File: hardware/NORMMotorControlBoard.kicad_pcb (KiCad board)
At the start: 2 copper layers, 2 parts, among them SW1 Reset, U1 Arduino Nano 33 BLE

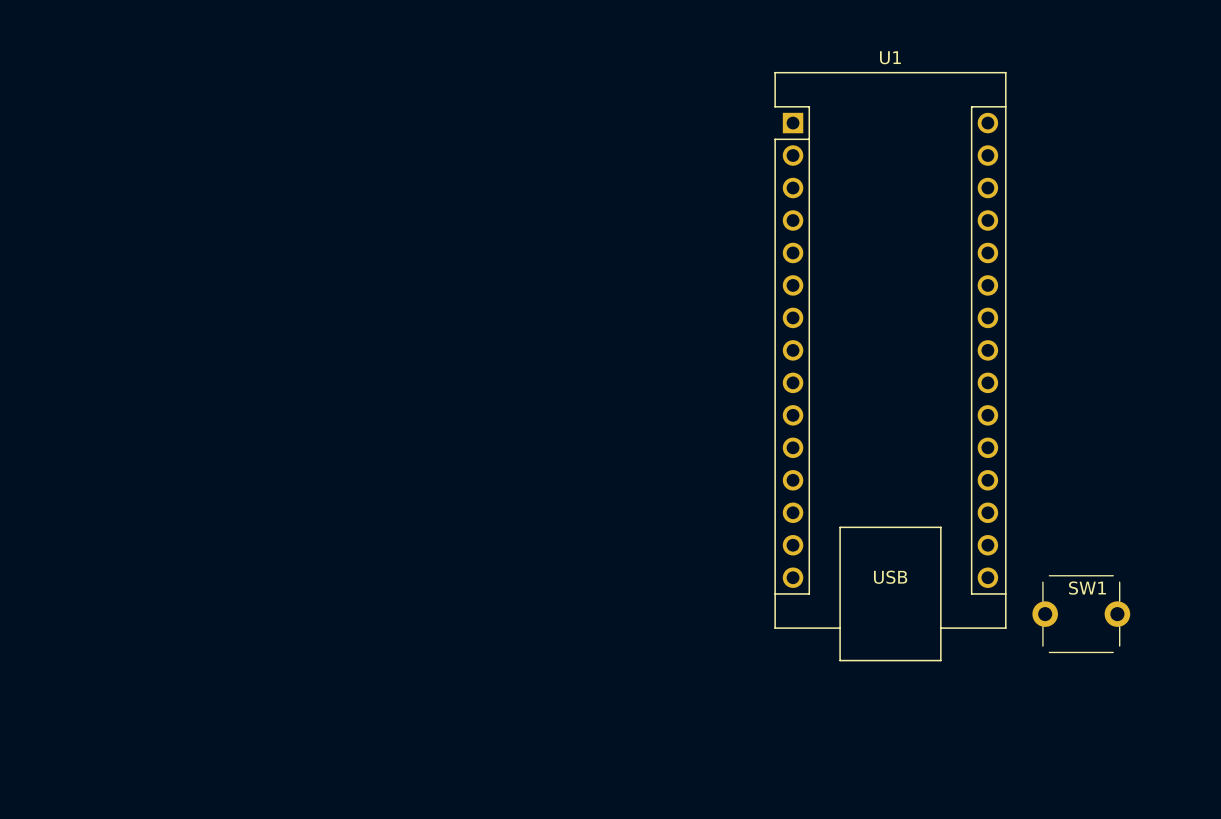
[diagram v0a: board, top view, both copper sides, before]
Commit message: Finished schematic and placed components
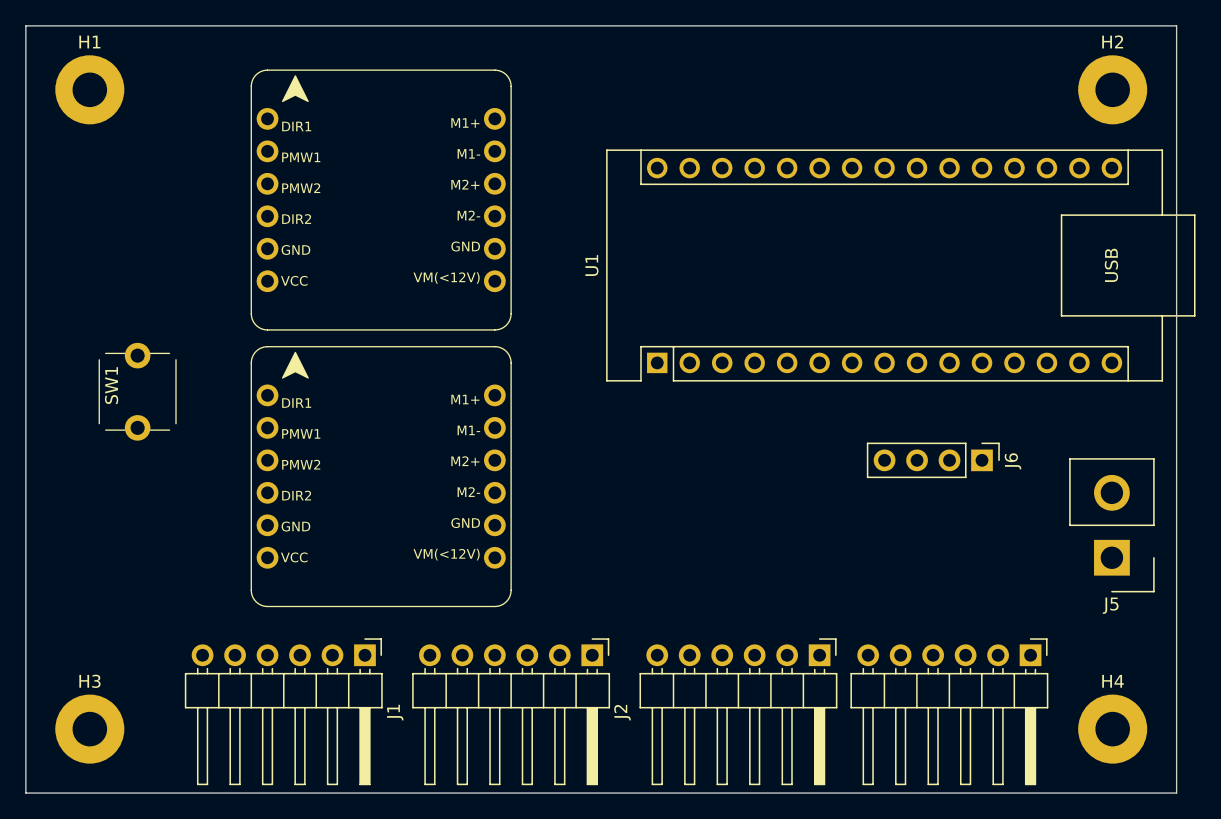
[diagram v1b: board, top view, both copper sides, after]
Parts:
- added H1: MountingHole_Pad, MountingHole:MountingHole_2.7mm_M2.5_Pad, F.Cu at (75.0, 65.0)
- added H2: MountingHole_Pad, MountingHole:MountingHole_2.7mm_M2.5_Pad, F.Cu at (155.0, 65.0)
- added H3: MountingHole_Pad, MountingHole:MountingHole_2.7mm_M2.5_Pad, F.Cu at (75.0, 115.0)
- added H4: MountingHole_Pad, MountingHole:MountingHole_2.7mm_M2.5_Pad, F.Cu at (155.0, 115.0)
- added J1: Front Left Motor, Connector_PinHeader_2.54mm:PinHeader_1x06_P2.54mm_Horizontal, F.Cu at (96.5, 109.2)
- added J2: Front Right Motor, Connector_PinHeader_2.54mm:PinHeader_1x06_P2.54mm_Horizontal, F.Cu at (114.3, 109.2)
- added J3: Back Left Motor, Connector_PinHeader_2.54mm:PinHeader_1x06_P2.54mm_Horizontal, F.Cu at (132.1, 109.2)
- added J4: Back Right Motor, Connector_PinHeader_2.54mm:PinHeader_1x06_P2.54mm_Horizontal, F.Cu at (148.6, 109.2)
- added J5: Conn_01x02_Socket, Connector_Samtec_HPM_THT:Samtec_HPM-02-01-x-S_Straight_1x02_Pitch5.08mm, F.Cu at (154.9, 101.6)
- added J6: Conn_01x04_Pin, Connector_PinHeader_2.54mm:PinHeader_1x04_P2.54mm_Vertical, F.Cu at (144.8, 94.0)
- added U2: Front Motors, DFRobot_DC_Motor_Driver_Shield:DFRobot_DC_Motor_Driver_Shield, F.Cu at (97.8, 95.3)
- added U3: Back Motors, DFRobot_DC_Motor_Driver_Shield:DFRobot_DC_Motor_Driver_Shield, F.Cu at (97.8, 73.7)
- moved SW1 75.8 mm to (78.7, 88.6), turned to 90 degrees
- moved U1 21.6 mm to (119.4, 86.4), turned to 90 degrees
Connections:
- U1 pad 15: unconnected-(U1-MISO-Pad15) -> D12
- U1 pad 16: unconnected-(U1-SCK-Pad16) -> D13
- U1 pad 23: unconnected-(U1-SDA/A4-Pad23) -> A4
- U1 pad 24: unconnected-(U1-SCL/A5-Pad24) -> A5
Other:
- board outline added: 90 x 60 mm

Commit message: Finished V1.0
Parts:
- moved J6 28.1 mm to (142.2, 66.0)
- moved U2 23.4 mm to (92.7, 72.4)
- moved U3 22.2 mm to (92.7, 95.3)
- moved SW1 2.54 mm to (76.2, 88.6), turned to 0 degrees
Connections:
- J6 pad 1: D12 -> D13
- J6 pad 2: D13 -> D12
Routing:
- net +5V: track 0.00 -> 254.7 mm
- net +3.3V: track 0.00 -> 105.9 mm
- net FL_ENC_B: track 0.00 -> 95.0 mm
- net FL_ENC_A: track 0.00 -> 92.5 mm
- net BL_DIR: track 0.00 -> 89.2 mm
- net BR_DIR: track 0.00 -> 75.5 mm
- net FR_ENC_B: track 0.00 -> 73.1 mm, vias 0 -> 1
- net FR_SPEED: track 0.00 -> 72.5 mm
- net FR_ENC_A: track 0.00 -> 70.5 mm, vias 0 -> 1
- net FR_DIR: track 0.00 -> 69.9 mm, vias 0 -> 1
- net FL_DIR: track 0.00 -> 68.0 mm
- net BR_SPEED: track 0.00 -> 59.5 mm
- net BL_SPEED: track 0.00 -> 56.6 mm
- net BL_ENC_B: track 0.00 -> 55.7 mm
- net FL_SPEED: track 0.00 -> 54.0 mm, vias 0 -> 1
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- added copper zone on B.Cu, net GND
- added copper zone on F.Cu, net GND
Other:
- outline, holes or cut-outs redrawn
- board text added: "(Neat Omnidirectional Robotic Module)"
- board text added: "5V"
- board text added: "A4"
- board text added: "A5"
- board text added: "Back Left"
- board text added: "Back Right"
- board text added: "D12"
- board text added: "D13"
- board text added: "ENC_A"
- board text added: "ENC_B"
- board text added: "Front Left"
- board text added: "Front Right"
- board text added: "GND"
- board text added: "M+"
- board text added: "M-"
- board text added: "N.O.R.M."
- board text added: "N.O.R.M. Motor Control Board github.com/HBoyd255/norm-motor-control-board V1.0 30/10/2024 Harry Boyd"
- board text added: "Project"
- board text added: "Reset"
- board text added: "VCC"

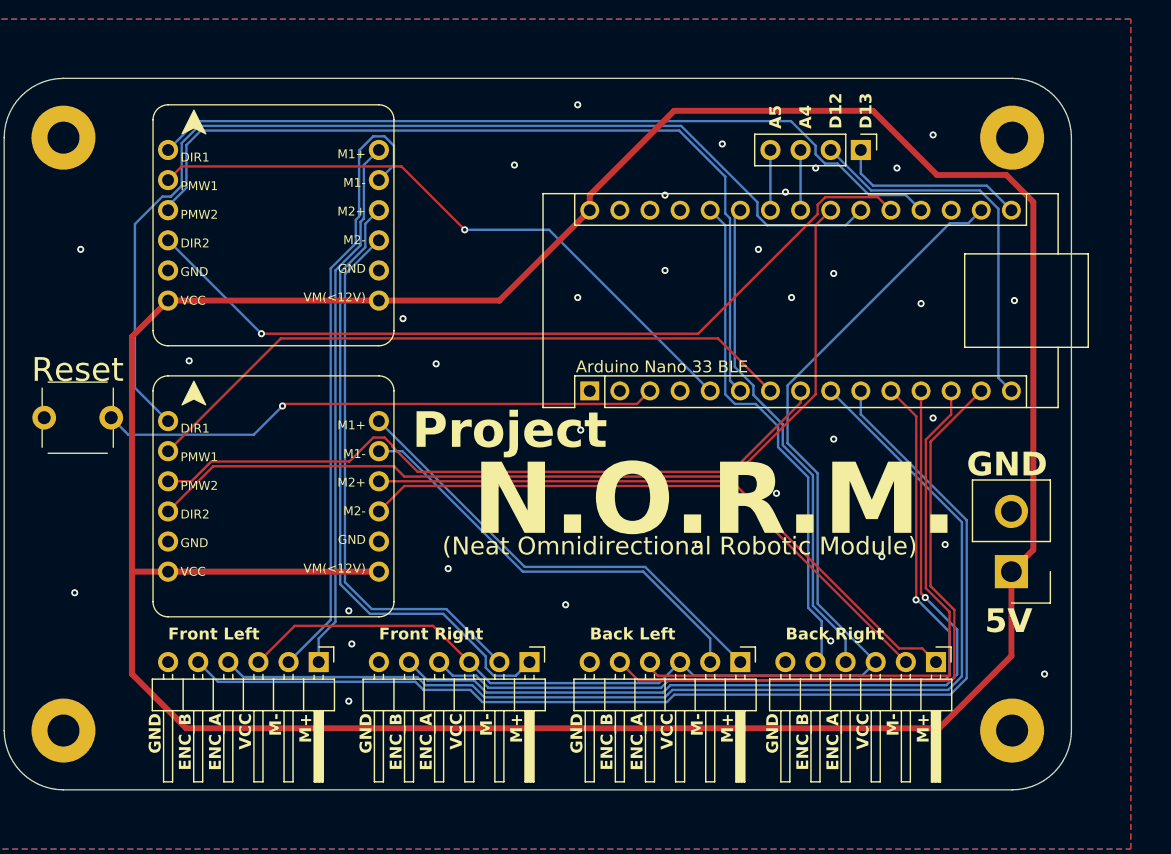
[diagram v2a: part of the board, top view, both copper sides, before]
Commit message: Added USB C and replaced components
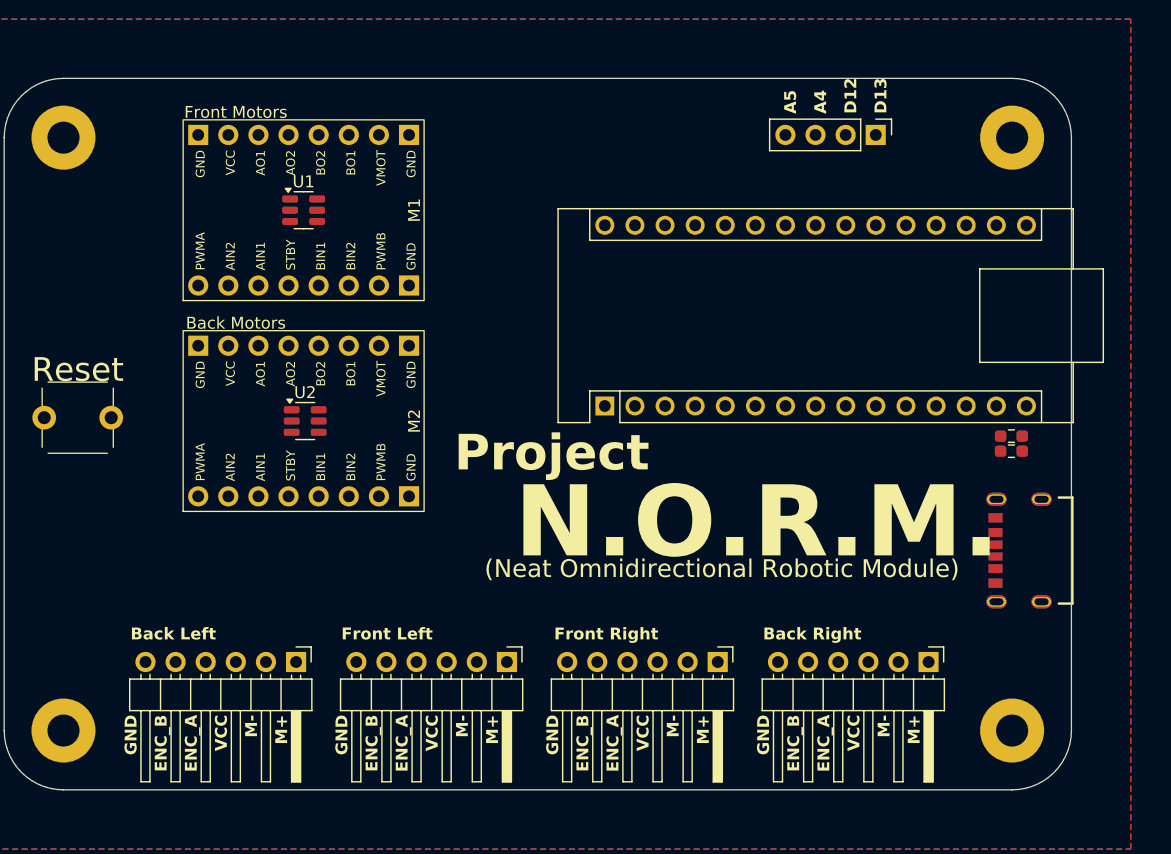
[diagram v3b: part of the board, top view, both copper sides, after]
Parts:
- removed the J2 at (114.3, 109.2)
- removed U3: Back Motors, DFRobot_DC_Motor_Driver_Shield:DFRobot_DC_Motor_Driver_Shield
- added A1: Arduino Nano 33 BLE, Module:Arduino_Nano, F.Cu at (120.7, 87.6)
- added J1: Back Left Motor, Connector_PinHeader_2.54mm:PinHeader_1x06_P2.54mm_Horizontal, F.Cu at (94.6, 109.2)
- added M1: Front Motors, Pololu_MD08A_Motor_Driver:Pololu_MD08A_Motor_Driver, F.Cu at (95.2, 71.1)
- added M2: Back Motors, Pololu_MD08A_Motor_Driver:Pololu_MD08A_Motor_Driver, F.Cu at (95.2, 88.9)
- added R3: 5.1k, Resistor_SMD:R_0603_1608Metric_Pad0.98x0.95mm_HandSolder, F.Cu at (154.9, 90.2)
- added R4: 5.1k, Resistor_SMD:R_0603_1608Metric_Pad0.98x0.95mm_HandSolder, F.Cu at (154.9, 91.4)
- J3: value Back Left Motor -> Front Right Motor
- J5: value Conn_01x02_Socket -> USB4125-GF-A_REVA2; footprint Connector_Samtec_HPM_THT:Samtec_HPM-02-01-x-S_Straight_1x02_Pitch5.08mm -> USB_C:USB_C
- U1: value Arduino Nano 33 BLE -> SN74LVC2G14DBV; footprint Module:Arduino_Nano -> Package_TO_SOT_SMD:SOT-23-6
- U2: value Front Motors -> SN74LVC2G14DBV; footprint DFRobot_DC_Motor_Driver_Shield:DFRobot_DC_Motor_Driver_Shield -> Package_TO_SOT_SMD:SOT-23-6
- moved U1 28.5 mm to (95.2, 71.1), turned to 0 degrees
- moved U2 16.7 mm to (95.4, 88.9)
- moved J2 15.9 mm to (112.4, 109.2)
- moved J5 2.49 mm to (156.7, 99.8), turned to 90 degrees
- moved J3 1.91 mm to (130.2, 109.2)
- moved J6 1.79 mm to (143.5, 64.8)
- moved J4 0.62 mm to (148.0, 109.2)
- renumbered J1 to J2
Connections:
- J2 pad 1: FL_M+ -> FR_M+
- J2 pad 2: FL_M- -> FR_M-
- J2 pad 4: FL_ENC_A -> FR_ENC_A
- J2 pad 5: FL_ENC_B -> FR_ENC_B
- SW1 pad 2: Net-(SW1-Pad2) -> Net-(A1-~{RESET}-Pad3)
- U1 pad 1: unconnected-(U1-TX1-Pad1) -> FL_DIR
- U1 pad 2: unconnected-(U1-RX1-Pad2) -> GND
- U1 pad 3: Net-(SW1-Pad2) -> FR_DIR
- U1 pad 4: GND -> /FR_DIR_INV
- U1 pad 5: FL_SPEED -> +5V
- U1 pad 6: FR_SPEED -> /FL_DIR_INV
- U2 pad 1: FL_DIR -> BL_DIR
- U2 pad 2: FL_SPEED -> GND
- U2 pad 3: FR_SPEED -> BR_DIR
- U2 pad 4: FR_DIR -> /BR_DIR_INV
- U2 pad 5: GND -> +5V
- U2 pad 6: +5V -> /BL_DIR_INV
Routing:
- net +5V: track 254.7 -> 0.00 mm
- net +3.3V: track 105.9 -> 0.00 mm
- net FL_ENC_B: track 95.0 -> 0.00 mm
- net FL_ENC_A: track 92.5 -> 0.00 mm
- net BL_DIR: track 89.2 -> 0.00 mm
- net BR_DIR: track 75.5 -> 0.00 mm
- net FR_ENC_B: track 73.1 -> 0.00 mm, vias 1 -> 0
- net FR_SPEED: track 72.5 -> 0.00 mm
- net FR_ENC_A: track 70.5 -> 0.00 mm, vias 1 -> 0
- net FR_DIR: track 69.9 -> 0.00 mm, vias 1 -> 0
- net FL_DIR: track 68.0 -> 0.00 mm
- net BR_SPEED: track 59.5 -> 0.00 mm
- net BL_SPEED: track 56.6 -> 0.00 mm
- net BL_ENC_B: track 55.7 -> 0.00 mm
- net FL_SPEED: track 54.0 -> 0.00 mm, vias 1 -> 0
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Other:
- board text added: "N.O.R.M. Motor Control Board github.com/HBoyd255/norm-motor-control-board V1.1 20/11/2024 Harry Boyd"
- board text removed: "5V"
- board text removed: "N.O.R.M. Motor Control Board github.com/HBoyd255/norm-motor-control-board V1.0 30/10/2024 Harry Boyd"

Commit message: Exported board v1.1
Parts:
- moved R4 0.38 mm to (154.9, 91.8)
- moved U1 0.13 mm to (95.4, 71.1)
- moved J5 0.09 mm to (156.6, 99.8)
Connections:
- J1 pad 1: FL_M+ -> BL_M+
- J1 pad 2: FL_M- -> BL_M-
- J1 pad 4: FL_ENC_A -> BL_ENC_A
- J1 pad 5: FL_ENC_B -> BL_ENC_B
- J2 pad 1: FR_M+ -> FL_M+
- J2 pad 2: FR_M- -> FL_M-
- J2 pad 4: FR_ENC_A -> FL_ENC_A
- J2 pad 5: FR_ENC_B -> FL_ENC_B
- J3 pad 1: BL_M+ -> FR_M+
- J3 pad 2: BL_M- -> FR_M-
- J3 pad 4: BL_ENC_A -> FR_ENC_A
- J3 pad 5: BL_ENC_B -> FR_ENC_B
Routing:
- net +3.3V: track 0.00 -> 202.1 mm
- net +5V: track 0.00 -> 131.2 mm, vias 0 -> 1
- net BL_DIR: track 0.00 -> 88.3 mm, vias 0 -> 2
- net Net-(A1-~{RESET}-Pad3): track 0.00 -> 88.0 mm
- net BL_ENC_B: track 0.00 -> 82.3 mm, vias 0 -> 1
- net FL_DIR: track 0.00 -> 77.1 mm, vias 0 -> 1
- net BL_ENC_A: track 0.00 -> 76.6 mm, vias 0 -> 1
- net BR_DIR: track 0.00 -> 71.1 mm, vias 0 -> 3
- net BL_SPEED: track 0.00 -> 64.7 mm, vias 0 -> 2
- net BR_M-: track 0.00 -> 62.4 mm
- net BR_M+: track 0.00 -> 61.5 mm
- net FL_M-: track 0.00 -> 60.6 mm
- net FR_DIR: track 0.00 -> 59.5 mm, vias 0 -> 2
- net FR_M-: track 0.00 -> 58.2 mm
- net FR_M+: track 0.00 -> 57.3 mm
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
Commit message: Placed components
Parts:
- removed M1: Front Motors, Pololu_MD08A_Motor_Driver:Pololu_MD08A_Motor_Driver
- removed M2: Back Motors, Pololu_MD08A_Motor_Driver:Pololu_MD08A_Motor_Driver
- added D1: LED, LED_SMD:LED_0603_1608Metric, F.Cu at (262.9, 188.7)
- added D2: LED, LED_SMD:LED_0603_1608Metric, F.Cu at (265.4, 188.7)
- added D3: LED, LED_SMD:LED_0603_1608Metric, F.Cu at (268.0, 188.7)
- added D4: LED, LED_SMD:LED_0603_1608Metric, F.Cu at (270.5, 188.7)
- added D5: LED, LED_SMD:LED_0603_1608Metric, F.Cu at (254.0, 230.8)
- added D6: LED, LED_SMD:LED_0603_1608Metric, F.Cu at (251.5, 230.8)
- added D7: LED, LED_SMD:LED_0603_1608Metric, F.Cu at (248.9, 230.8)
- added D8: LED, LED_SMD:LED_0603_1608Metric, F.Cu at (246.4, 230.8)
- added J7: SparePins, Connector_PinHeader_2.54mm:PinHeader_1x05_P2.54mm_Vertical, F.Cu at (285.8, 266.0)
- added R1: 1k, Resistor_SMD:R_0603_1608Metric, F.Cu at (262.9, 191.8)
- added R2: 1k, Resistor_SMD:R_0603_1608Metric, F.Cu at (265.4, 191.8)
- added R5: 1k, Resistor_SMD:R_0603_1608Metric, F.Cu at (254.0, 227.8)
- added R6: 1k, Resistor_SMD:R_0603_1608Metric, F.Cu at (251.5, 227.8)
- added R7: 1k, Resistor_SMD:R_0603_1608Metric, F.Cu at (248.9, 227.8)
- added R8: 1k, Resistor_SMD:R_0603_1608Metric, F.Cu at (246.4, 227.8)
- added U3: 74HC595, Package_DIP:DIP-16_W7.62mm, F.Cu at (261.1, 223.8)
- J1: value Back Left Motor -> Front Right Motor; footprint Connector_PinHeader_2.54mm:PinHeader_1x06_P2.54mm_Horizontal -> Connector_JST:JST_PH_S6B-PH-K_1x06_P2.00mm_Horizontal
- J2: footprint Connector_PinHeader_2.54mm:PinHeader_1x06_P2.54mm_Horizontal -> Connector_JST:JST_PH_S6B-PH-K_1x06_P2.00mm_Horizontal
- J3: value Front Right Motor -> Back Right Motor; footprint Connector_PinHeader_2.54mm:PinHeader_1x06_P2.54mm_Horizontal -> Connector_JST:JST_PH_S6B-PH-K_1x06_P2.00mm_Horizontal
- J4: value Back Right Motor -> Back Left Motor; footprint Connector_PinHeader_2.54mm:PinHeader_1x06_P2.54mm_Horizontal -> Connector_JST:JST_PH_S6B-PH-K_1x06_P2.00mm_Horizontal
- J5: value USB4125-GF-A_REVA2 -> Conn_01x02_Socket; footprint USB_C:USB_C -> Connector_Samtec_HPM_THT:Samtec_HPM-02-01-x-S_Straight_1x02_Pitch5.08mm
- J6: value Conn_01x04_Pin -> SparePins; footprint Connector_PinHeader_2.54mm:PinHeader_1x04_P2.54mm_Vertical -> Connector_PinHeader_2.54mm:PinHeader_1x05_P2.54mm_Horizontal
- R3, R4: value 5.1k -> 1k; footprint Resistor_SMD:R_0603_1608Metric_Pad0.98x0.95mm_HandSolder -> Resistor_SMD:R_0603_1608Metric
- U1: value SN74LVC2G14DBV -> Front Driver; footprint Package_TO_SOT_SMD:SOT-23-6 -> L298N:L298N
- U2: value SN74LVC2G14DBV -> Back Driver; footprint Package_TO_SOT_SMD:SOT-23-6 -> L298N:L298N
- moved SW1 259.5 mm to (248.0, 283.1)
- moved U2 232.8 mm to (258.7, 254.8), turned to 180 degrees
- moved J6 221.5 mm to (228.6, 269.3), turned to 180 degrees
- moved H3 219.7 mm to (220.0, 280.0)
- moved J5 214.6 mm to (265.0, 285.0), turned to -90 degrees
- moved J4 213.6 mm to (274.2, 281.5), turned to 0 degrees
- moved J3 197.5 mm to (227.3, 281.1), turned to 0 degrees
- moved H4 194.7 mm to (285.0, 260.0)
- moved U1 187.8 mm to (258.1, 164.9)
- moved H1 177.6 mm to (225.0, 160.0)
- moved J2 171.2 mm to (281.0, 139.0), turned to 180 degrees
- moved H2 161.0 mm to (285.0, 160.0)
- moved A1 158.5 mm to (217.8, 212.8), turned to 0 degrees
- moved J1 153.3 mm to (245.0, 139.0), turned to 180 degrees
- moved R4 152.8 mm to (270.5, 191.8), turned to -90 degrees
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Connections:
- A1 pad 10: FL_ENC_B -> FL_ENC_SEC
- A1 pad 11: FR_ENC_A -> FR_ENC_PRI
- A1 pad 12: FR_ENC_B -> FR_ENC_SEC
- A1 pad 13: BL_ENC_A -> BL_ENC_PRI
- A1 pad 14: BL_ENC_B -> BL_ENC_SEC
- A1 pad 19: FL_DIR -> SR_DATA
- A1 pad 20: FR_DIR -> SR_LATCH
- A1 pad 21: BL_DIR -> SR_CLOCK
- A1 pad 22: BR_DIR -> A3
- A1 pad 25: BR_ENC_A -> BR_ENC_PRI
- A1 pad 26: BR_ENC_B -> BR_ENC_SEC
- A1 pad 9: FL_ENC_A -> FL_ENC_PRI
- J1 pad 1: BL_M+ -> FR_M1
- J1 pad 2: BL_M- -> GND
- J1 pad 3: +3.3V -> FR_ENC_SEC
- J1 pad 4: BL_ENC_A -> FR_ENC_PRI
- J1 pad 5: BL_ENC_B -> +3.3V
- J1 pad 6: GND -> FR_M2
- J2 pad 1: FL_M+ -> FL_M1
- J2 pad 2: FL_M- -> GND
- J2 pad 3: +3.3V -> FL_ENC_PRI
- J2 pad 4: FL_ENC_A -> FL_ENC_SEC
- J2 pad 5: FL_ENC_B -> +3.3V
- J2 pad 6: GND -> FL_M2
- J3 pad 1: FR_M+ -> BR_M1
- J3 pad 2: FR_M- -> GND
- J3 pad 3: +3.3V -> BR_ENC_SEC
- J3 pad 4: FR_ENC_A -> BR_ENC_PRI
- J3 pad 5: FR_ENC_B -> +3.3V
- J3 pad 6: GND -> BR_M2
- J4 pad 1: BR_M+ -> BL_M1
- J4 pad 2: BR_M- -> GND
- J4 pad 3: +3.3V -> BL_ENC_PRI
- J4 pad 4: BR_ENC_A -> BL_ENC_SEC
- J4 pad 5: BR_ENC_B -> +3.3V
- J4 pad 6: GND -> BL_M2
- J6 pad 1: D13 -> +3.3V
- J6 pad 2: D12 -> GND
- J6 pad 3: A4 -> A3
- J6 pad 4: A5 -> A4
- R3 pad 1: GND -> Net-(D3-K)
- R3 pad 2: Net-(J5-CC1) -> GND
- R4 pad 1: GND -> Net-(D4-K)
- R4 pad 2: Net-(J5-CC2) -> GND
- U1 pad 1: FL_DIR -> FR_M1
- U1 pad 2: GND -> FR_M2
- U1 pad 3: FR_DIR -> +12V
- U1 pad 4: /FR_DIR_INV -> GND
- U1 pad 6: /FL_DIR_INV -> FR_SPEED
- U2 pad 1: BL_DIR -> BL_M2
- U2 pad 2: GND -> BL_M1
- U2 pad 3: BR_DIR -> +12V
- U2 pad 4: /BR_DIR_INV -> GND
- U2 pad 6: /BL_DIR_INV -> BL_SPEED
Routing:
- net +3.3V: track 202.1 -> 0.00 mm
- net +5V: track 131.2 -> 0.00 mm, vias 1 -> 0
- net BL_DIR: track 88.3 -> 0.00 mm, vias 2 -> 0
- net Net-(A1-~{RESET}-Pad3): track 88.0 -> 0.00 mm
- net BL_ENC_B: track 82.3 -> 0.00 mm, vias 1 -> 0
- net FL_DIR: track 77.1 -> 0.00 mm, vias 1 -> 0
- net BL_ENC_A: track 76.6 -> 0.00 mm, vias 1 -> 0
- net BR_DIR: track 71.1 -> 0.00 mm, vias 3 -> 0
- net BL_SPEED: track 64.7 -> 0.00 mm, vias 2 -> 0
- net BR_M-: track 62.4 -> 0.00 mm
- net BR_M+: track 61.5 -> 0.00 mm
- net FL_M-: track 60.6 -> 0.00 mm
- net FR_DIR: track 59.5 -> 0.00 mm, vias 2 -> 0
- net FR_M-: track 58.2 -> 0.00 mm
- net FR_M+: track 57.3 -> 0.00 mm
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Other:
- board size 90 x 60 mm -> 75 x 160 mm
- board text added: "12V"
- board text added: "3.3V"
- board text added: "3.3v"
- board text added: "5V"
- board text added: "A3"
- board text added: "N.O.R.M. Motor Control Board github.com/HBoyd255/norm-motor-control-board V1.2 17/02/2025 Harry Boyd"
- board text removed: "Back Left"
- board text removed: "Back Right"
- board text removed: "ENC_A"
- board text removed: "ENC_B"
- board text removed: "Front Left"
- board text removed: "Front Right"
- board text removed: "M+"
- board text removed: "M-"
- board text removed: "N.O.R.M. Motor Control Board github.com/HBoyd255/norm-motor-control-board V1.1 20/11/2024 Harry Boyd"
- board text removed: "Reset"
- board text removed: "VCC"
